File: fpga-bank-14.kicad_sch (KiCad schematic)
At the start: 20 parts, among them Q4 BSS138PW, Q5 BSS138PW, Q6 BSS138PW, Q7 BSS138PW, Q8 BSS138PW, U4 XC7K160T-FFG676

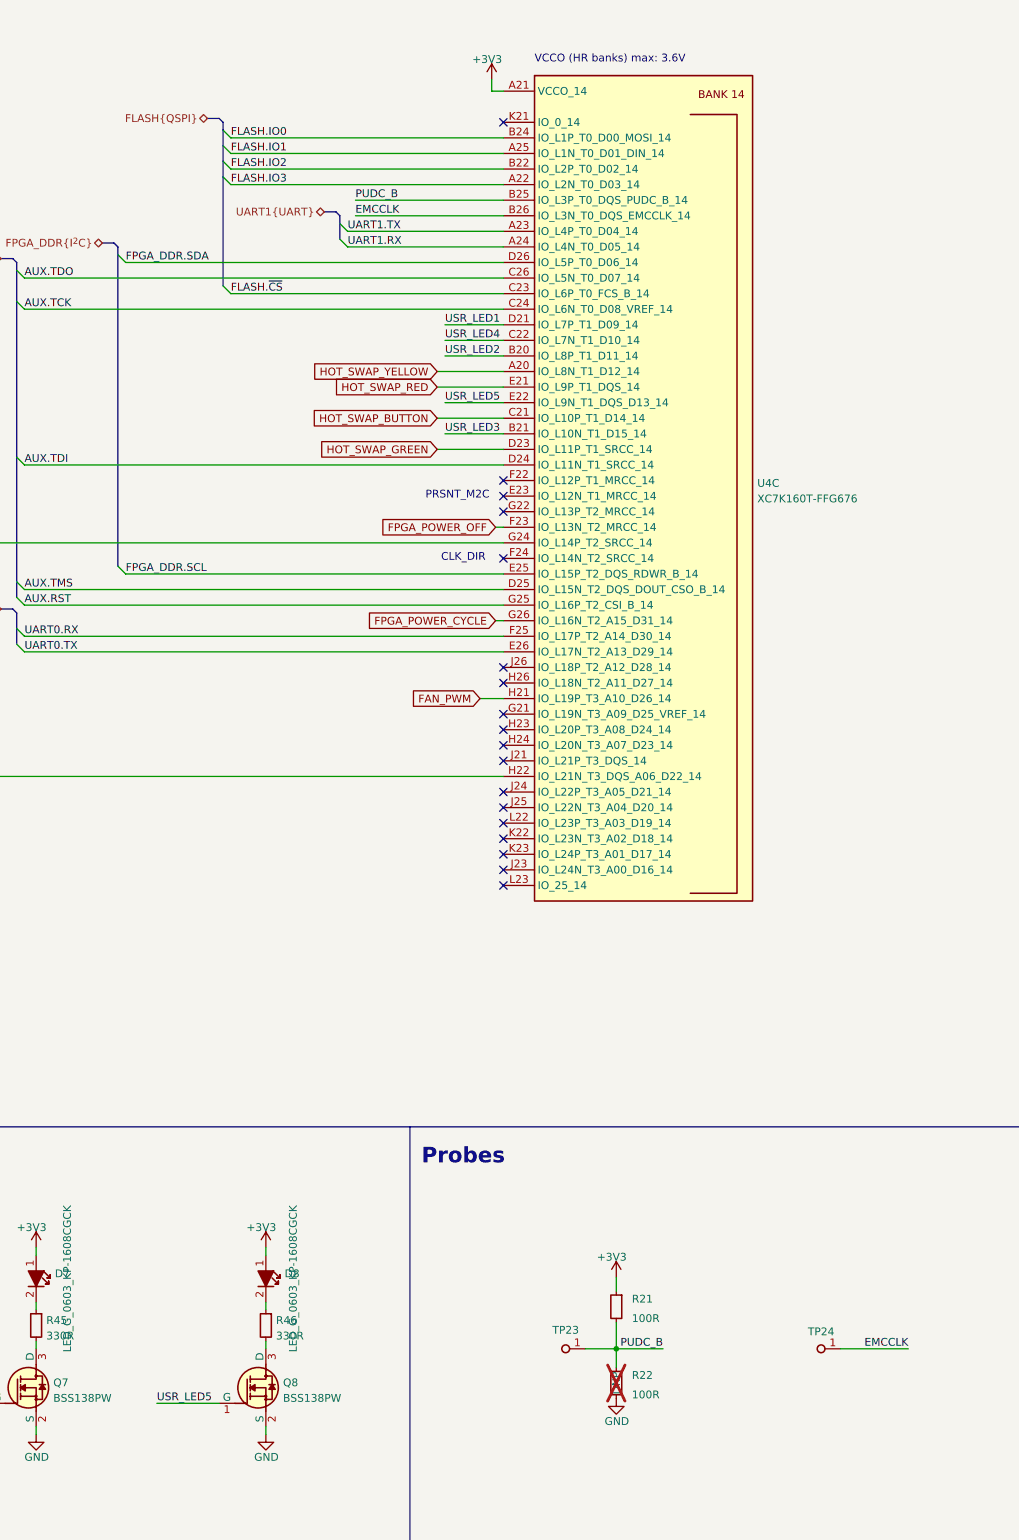
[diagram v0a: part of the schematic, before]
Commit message: [#66311] Add XCAU25P. Reconnect configuration bank 0
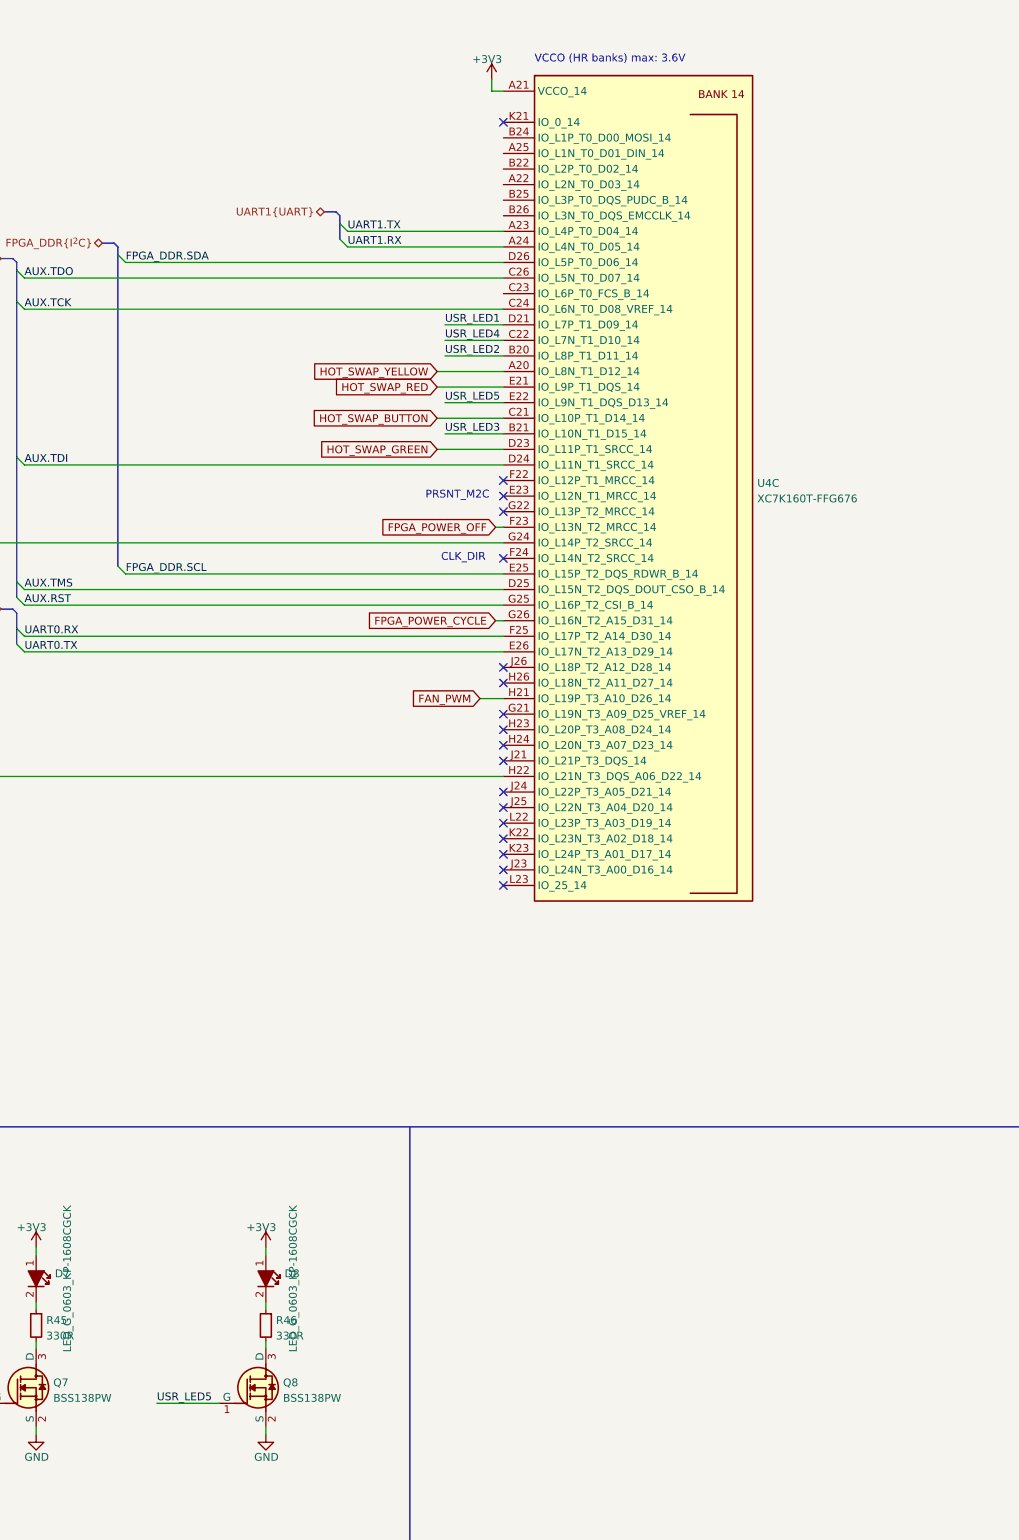
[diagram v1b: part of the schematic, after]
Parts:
- removed R21, R22: R_100R_0402, antmicro-footprints:R_0402_1005Metric, symbol antmicroResistors0402:R_100R_0402
- removed TP23, TP24: TP_1mm_SMD, antmicro-footprints:TP_SMD_1mm, symbol antmicroTestPoints:TP_1mm_SMD
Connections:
- net EMCCLK: no longer names the net of U4.B26 (IO_L3N_T0_DQS_EMCCLK_14)
- net FLASH.IO0: no longer names the net of U4.B24 (IO_L1P_T0_D00_MOSI_14)
- net FLASH.IO1: no longer names the net of U4.A25 (IO_L1N_T0_D01_DIN_14)
- net FLASH.IO2: no longer names the net of U4.B22 (IO_L2P_T0_D02_14)
- net FLASH.IO3: no longer names the net of U4.A22 (IO_L2N_T0_D03_14)
- net FLASH.~{CS}: no longer names the net of U4.C23 (IO_L6P_T0_FCS_B_14)
- net PUDC_B: no longer names the net of U4.B25 (IO_L3P_T0_DQS_PUDC_B_14)
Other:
- note removed: "Probes"

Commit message: [#65754] Rename project
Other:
- title: SO-DIMM DDR5 Tester -> RDIMM DDR5 Tester
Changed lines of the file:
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@@
   (paper "A3")
   (title_block
-    (title "SO-DIMM DDR5 Tester")
-    (date "2024-04-23")
-    (rev "1.2.0")
+    (title "RDIMM DDR5 Tester")
+    (date "2024-09-26")
+    (rev "2.0.0")
     (comment 1 "www.antmicro.com")
     (comment 2 "Antmicro Ltd")
@@
     (pin "2")
     (instances
-      (project "rdimm-ddr5-tester-ultrascale-plus"
+      (project "data-center-rdimm-ddr5-tester"
         (path "/1faa6543-e26a-4449-8bac-ee14b9f19e5f/34ebf93d-6b28-4c40-a799-aace59d6d135"
           (reference "R45") (unit 1)
@@
     (pin "3")
     (instances
-      (project "rdimm-ddr5-tester-ultrascale-plus"
+      (project "data-center-rdimm-ddr5-tester"
         (path "/1faa6543-e26a-4449-8bac-ee14b9f19e5f/34ebf93d-6b28-4c40-a799-aace59d6d135"
           (reference "Q7") (unit 1)
@@
     (pin "3")
     (instances
-      (project "rdimm-ddr5-tester-ultrascale-plus"
+      (project "data-center-rdimm-ddr5-tester"
         (path "/1faa6543-e26a-4449-8bac-ee14b9f19e5f/34ebf93d-6b28-4c40-a799-aace59d6d135"
           (reference "Q4") (unit 1)
@@
     (pin "1")
     (instances
-      (project "rdimm-ddr5-tester-ultrascale-plus"
+      (project "data-center-rdimm-ddr5-tester"
         (path "/1faa6543-e26a-4449-8bac-ee14b9f19e5f/34ebf93d-6b28-4c40-a799-aace59d6d135"
           (reference "#PWR0237") (unit 1)
@@
     (pin "2")
     (instances
-      (project "rdimm-ddr5-tester-ultrascale-plus"
+      (project "data-center-rdimm-ddr5-tester"
         (path "/1faa6543-e26a-4449-8bac-ee14b9f19e5f/34ebf93d-6b28-4c40-a799-aace59d6d135"
           (reference "R46") (unit 1)
@@
     (pin "1")
     (instances
-      (project "rdimm-ddr5-tester-ultrascale-plus"
+      (project "data-center-rdimm-ddr5-tester"
         (path "/1faa6543-e26a-4449-8bac-ee14b9f19e5f/34ebf93d-6b28-4c40-a799-aace59d6d135"
           (reference "#PWR0427") (unit 1)
@@
     (pin "1")
     (instances
-      (project "rdimm-ddr5-tester-ultrascale-plus"
+      (project "data-center-rdimm-ddr5-tester"
         (path "/1faa6543-e26a-4449-8bac-ee14b9f19e5f/34ebf93d-6b28-4c40-a799-aace59d6d135"
           (reference "#PWR0428") (unit 1)
@@
     (pin "1")
     (instances
-      (project "rdimm-ddr5-tester-ultrascale-plus"
+      (project "data-center-rdimm-ddr5-tester"
         (path "/1faa6543-e26a-4449-8bac-ee14b9f19e5f/34ebf93d-6b28-4c40-a799-aace59d6d135"
           (reference "#PWR0433") (unit 1)
@@
     (pin "1")
     (instances
-      (project "rdimm-ddr5-tester-ultrascale-plus"
+      (project "data-center-rdimm-ddr5-tester"
         (path "/1faa6543-e26a-4449-8bac-ee14b9f19e5f/34ebf93d-6b28-4c40-a799-aace59d6d135"
           (reference "#PWR0435") (unit 1)
@@
     (pin "2")
     (instances
-      (project "rdimm-ddr5-tester-ultrascale-plus"
+      (project "data-center-rdimm-ddr5-tester"
         (path "/1faa6543-e26a-4449-8bac-ee14b9f19e5f/34ebf93d-6b28-4c40-a799-aace59d6d135"
           (reference "D6") (unit 1)
@@
     (pin "1")
     (instances
-      (project "rdimm-ddr5-tester-ultrascale-plus"
+      (project "data-center-rdimm-ddr5-tester"
         (path "/1faa6543-e26a-4449-8bac-ee14b9f19e5f/34ebf93d-6b28-4c40-a799-aace59d6d135"
           (reference "#PWR0430") (unit 1)
@@
     (pin "T6")
     (instances
-      (project "rdimm-ddr5-tester-ultrascale-plus"
+      (project "data-center-rdimm-ddr5-tester"
         (path "/1faa6543-e26a-4449-8bac-ee14b9f19e5f/34ebf93d-6b28-4c40-a799-aace59d6d135"
           (reference "U4") (unit 3)
@@
     (pin "3")
     (instances
-      (project "rdimm-ddr5-tester-ultrascale-plus"
+      (project "data-center-rdimm-ddr5-tester"
         (path "/1faa6543-e26a-4449-8bac-ee14b9f19e5f/34ebf93d-6b28-4c40-a799-aace59d6d135"
           (reference "Q8") (unit 1)
@@
     (pin "2")
     (instances
-      (project "rdimm-ddr5-tester-ultrascale-plus"
+      (project "data-center-rdimm-ddr5-tester"
         (path "/1faa6543-e26a-4449-8bac-ee14b9f19e5f/34ebf93d-6b28-4c40-a799-aace59d6d135"
           (reference "D7") (unit 1)
@@
     (pin "1")
     (instances
-      (project "rdimm-ddr5-tester-ultrascale-plus"
+      (project "data-center-rdimm-ddr5-tester"
         (path "/1faa6543-e26a-4449-8bac-ee14b9f19e5f/34ebf93d-6b28-4c40-a799-aace59d6d135"
           (reference "#PWR0434") (unit 1)
@@
     (pin "2")
     (instances
-      (project "rdimm-ddr5-tester-ultrascale-plus"
+      (project "data-center-rdimm-ddr5-tester"
         (path "/1faa6543-e26a-4449-8bac-ee14b9f19e5f/34ebf93d-6b28-4c40-a799-aace59d6d135"
           (reference "R41") (unit 1)
@@
     (pin "1")
     (instances
-      (project "rdimm-ddr5-tester-ultrascale-plus"
+      (project "data-center-rdimm-ddr5-tester"
         (path "/1faa6543-e26a-4449-8bac-ee14b9f19e5f/34ebf93d-6b28-4c40-a799-aace59d6d135"
           (reference "#PWR0431") (unit 1)
@@
     (pin "2")
     (instances
-      (project "rdimm-ddr5-tester-ultrascale-plus"
+      (project "data-center-rdimm-ddr5-tester"
         (path "/1faa6543-e26a-4449-8bac-ee14b9f19e5f/34ebf93d-6b28-4c40-a799-aace59d6d135"
           (reference "D4") (unit 1)
@@
     (pin "1")
     (instances
-      (project "rdimm-ddr5-tester-ultrascale-plus"
+      (project "data-center-rdimm-ddr5-tester"
         (path "/1faa6543-e26a-4449-8bac-ee14b9f19e5f/34ebf93d-6b28-4c40-a799-aace59d6d135"
           (reference "#PWR0426") (unit 1)
@@
     (pin "3")
     (instances
-      (project "rdimm-ddr5-tester-ultrascale-plus"
+      (project "data-center-rdimm-ddr5-tester"
         (path "/1faa6543-e26a-4449-8bac-ee14b9f19e5f/34ebf93d-6b28-4c40-a799-aace59d6d135"
           (reference "Q5") (unit 1)
@@
     (pin "3")
     (instances
-      (project "rdimm-ddr5-tester-ultrascale-plus"
+      (project "data-center-rdimm-ddr5-tester"
         (path "/1faa6543-e26a-4449-8bac-ee14b9f19e5f/34ebf93d-6b28-4c40-a799-aace59d6d135"
           (reference "Q6") (unit 1)
@@
     (pin "1")
     (instances
-      (project "rdimm-ddr5-tester-ultrascale-plus"
+      (project "data-center-rdimm-ddr5-tester"
         (path "/1faa6543-e26a-4449-8bac-ee14b9f19e5f/34ebf93d-6b28-4c40-a799-aace59d6d135"
           (reference "#PWR0432") (unit 1)
@@
     (pin "2")
     (instances
-      (project "rdimm-ddr5-tester-ultrascale-plus"
+      (project "data-center-rdimm-ddr5-tester"
         (path "/1faa6543-e26a-4449-8bac-ee14b9f19e5f/34ebf93d-6b28-4c40-a799-aace59d6d135"
           (reference "R40") (unit 1)
@@
     (pin "1")
     (instances
-      (project "rdimm-ddr5-tester-ultrascale-plus"
+      (project "data-center-rdimm-ddr5-tester"
         (path "/1faa6543-e26a-4449-8bac-ee14b9f19e5f/34ebf93d-6b28-4c40-a799-aace59d6d135"
           (reference "#PWR0429") (unit 1)
@@
     (pin "2")
     (instances
-      (project "rdimm-ddr5-tester-ultrascale-plus"
+      (project "data-center-rdimm-ddr5-tester"
         (path "/1faa6543-e26a-4449-8bac-ee14b9f19e5f/34ebf93d-6b28-4c40-a799-aace59d6d135"
           (reference "D5") (unit 1)
@@
     (pin "2")
     (instances
-      (project "rdimm-ddr5-tester-ultrascale-plus"
+      (project "data-center-rdimm-ddr5-tester"
         (path "/1faa6543-e26a-4449-8bac-ee14b9f19e5f/34ebf93d-6b28-4c40-a799-aace59d6d135"
           (reference "R42") (unit 1)
@@
     (pin "2")
     (instances
-      (project "rdimm-ddr5-tester-ultrascale-plus"
+      (project "data-center-rdimm-ddr5-tester"
         (path "/1faa6543-e26a-4449-8bac-ee14b9f19e5f/34ebf93d-6b28-4c40-a799-aace59d6d135"
           (reference "D8") (unit 1)
